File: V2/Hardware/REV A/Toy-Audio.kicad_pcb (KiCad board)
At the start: 2 copper layers, 24 x 14 mm, 24 parts, among them J1 CONN_01X02, J2 CONN_01X04, J3 CONN_01X03, J4 CONN_01X03, J5 CONN_01X04, U1 XC6206P332MR, U2 STM32F030F4P6, U3 W25Q32FVSIG, U4 TS4890

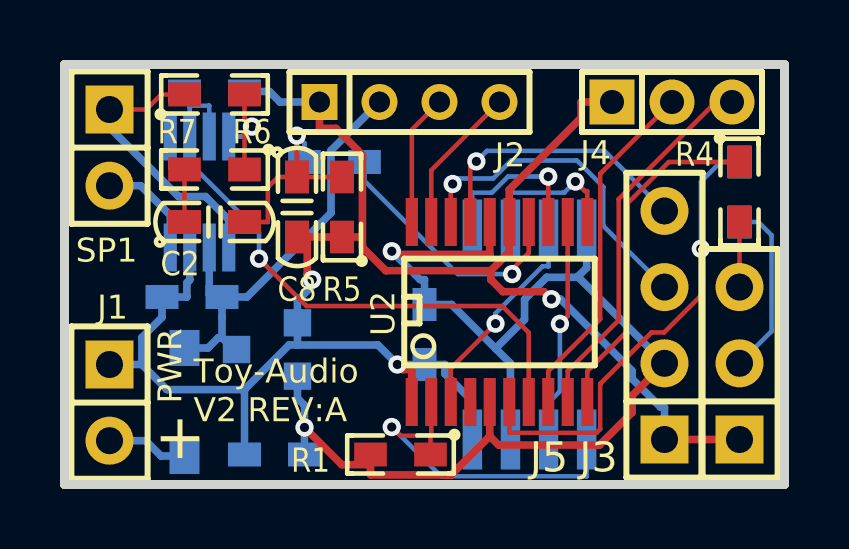
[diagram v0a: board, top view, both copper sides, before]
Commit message: Modified PCB layout, improved hand solderability.
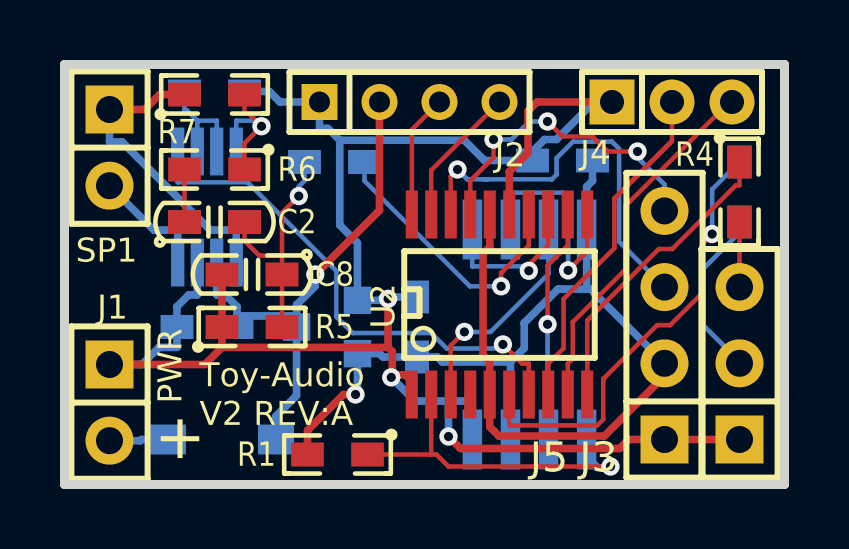
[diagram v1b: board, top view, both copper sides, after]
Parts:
- R3: value 1k8 -> 910R
- R5: value 1k8 -> D.N.P
- moved C7 7.40 mm to (112.6, 92.2), turned to 180 degrees
- moved C6 6.37 mm to (107.8, 97.8), turned to 90 degrees
- moved R5 5.00 mm to (102.2, 97.8), turned to 0 degrees
- moved C8 2.70 mm to (102.2, 96.0), turned to 180 degrees
- moved U1 2.14 mm to (104.8, 97.8)
- moved R1 2.10 mm to (105.1, 102.0)
- moved D1 1.77 mm to (101.2, 101.5), turned to 180 degrees
- moved C10 1.12 mm to (100.8, 97.8)
- moved U4 0.56 mm to (100.8, 93.8)
- moved U2 0.25 mm to (110.5, 97.0)
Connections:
- net Net-(R7-Pad1) renamed /SP+
- net Net-(SP1-Pad2) renamed /SP-
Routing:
- net GND: track 62.7 -> 66.6 mm
- net VDD: track 42.0 -> 38.6 mm, vias 2 -> 1
- net /SCK1: track 5.10 -> 7.77 mm
- net VCC: track 14.8 -> 17.3 mm, vias 0 -> 1
- net /USART1_TX: track 11.7 -> 14.2 mm
- net /SDA1: track 11.2 -> 13.3 mm
- net /SCL1: track 9.35 -> 11.1 mm, vias 1 -> 3
- net Net-(R6-Pad1): track 3.62 -> 5.00 mm
- net /LED: track 11.5 -> 10.2 mm
- net Net-(C2-Pad2): track 6.92 -> 7.89 mm
- net /SP+: track 9.48 -> 10.3 mm
- net /nMUTE: track 18.1 -> 17.3 mm
- net Net-(D1-PadA): track 2.71 -> 1.97 mm
- net Net-(C1-Pad1): track 3.25 -> 3.90 mm
- net /PWM: track 8.80 -> 9.41 mm
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
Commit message: Added Standby mode to software V1. Modified hardware to support Standby (add pull up/down resistors) todo hardware V3
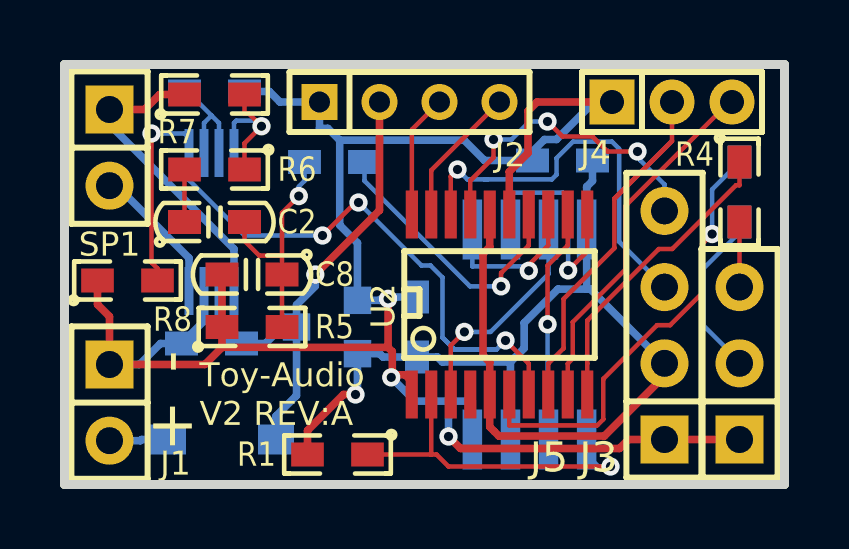
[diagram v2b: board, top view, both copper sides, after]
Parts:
- added R8: 47k, MvdL:R0603, F.Cu at (98.1, 96.2)
- U4: footprint myfootprints VDL:SSOP-8 -> MvdL:MSOP8
- moved C10 0.57 mm to (100.9, 98.3)
- moved U4 0.47 mm to (100.9, 94.2)
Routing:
- net /nMUTE: track 17.3 -> 26.9 mm, vias 1 -> 4
- net GND: track 66.6 -> 68.5 mm
- net /SP-: track 3.97 -> 4.75 mm
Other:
- board text added: "-"
- board text added: "SP1"

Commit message: Improved Wake-up pin stability WKUP1. modiefied schematic files. Software V1 is compatible with hardware V2
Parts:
- added R9: 10k, MvdL:R0603, B.Cu at (119.3, 100.8)
- R8: value 47k -> 100k
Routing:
- net GND: track 68.5 -> 71.4 mm
- net Net-(J3-Pad2): track 5.70 -> 6.83 mm
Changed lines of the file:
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@@
 (kicad_pcb (version 4) (host pcbnew 4.0.0-rc2-stable)
   (general
-    (links 59)
+    (links 61)
     (no_connects 0)
     (area 95.849999 88.849999 120.150001 103.150001)
     (thickness 1.6)
     (drawings 9)
-    (tracks 305)
+    (tracks 312)
     (zones 0)
-    (modules 25)
+    (modules 26)
     (nets 28)
   )
@@
       (effects (font (size 0.8128 0.7112) (thickness 0.1524)))
     )
-    (fp_text value 47k (at 0.0254 1.143) (layer F.Fab)
+    (fp_text value 100k (at 0.0254 1.143) (layer F.Fab)
       (effects (font (size 0.50038 0.50038) (thickness 0.10922)))
     )
@@
     )
   )
+  (module MvdL:R0603 (layer B.Cu)
+    (at 119.3 100.75 90)
+    (attr smd)
+    (fp_text reference R9 (at 3 0 360) (layer B.SilkS)
+      (effects (font (size 0.8128 0.7112) (thickness 0.1524)) (justify mirror))
+    )
+    (fp_text value 10k (at 0.0254 -1.143 90) (layer B.Fab)
+      (effects (font (size 0.50038 0.50038) (thickness 0.10922)) (justify mirror))
+    )
+    (fp_line (start -1.6002 0.635) (end -1.7272 0.635) (layer B.SilkS) (width 0.1524))
+    (fp_line (start -1.7772 0.635) (end -1.7772 -0.635) (layer B.SilkS) (width 0.1524))
+    (fp_line (start -1.7272 -0.635) (end -1.6256 -0.635) (layer B.SilkS) (width 0.1524))
+    (fp_line (start 1.6002 0.635) (end 1.7272 0.635) (layer B.SilkS) (width 0.1524))
+    (fp_line (start 1.7772 0.635) (end 1.7772 -0.635) (layer B.SilkS) (width 0.1524))
+    (fp_line (start 1.7272 -0.635) (end 1.6002 -0.635) (layer B.SilkS) (width 0.1524))
+    (fp_line (start 0.5814 0.635) (end 1.7752 0.635) (layer B.SilkS) (width 0.1524))
+    (fp_line (start 0.5814 -0.635) (end 1.7752 -0.635) (layer B.SilkS) (width 0.1524))
+    (fp_line (start -0.5564 -0.635) (end -1.7502 -0.635) (layer B.SilkS) (width 0.1524))
+    (fp_line (start -0.5814 0.635) (end -1.7752 0.635) (layer B.SilkS) (width 0.1524))
+    (fp_circle (center -1.7974 -0.658) (end -1.7974 -0.531) (layer B.SilkS) (width 0.1524))
+    (pad 1 smd rect (at -1 0 90) (size 1.0922 0.8) (layers B.Cu B.Paste B.Mask)
+      (net 1 GND) (clearance 0.1524))
+    (pad 2 smd rect (at 1 0 90) (size 1.0922 0.8) (layers B.Cu B.Paste B.Mask)
+      (net 16 "Net-(J3-Pad2)") (clearance 0.1524))
+    (model smd/chip_cms.wrl
+      (at (xyz 0 0 0))
+      (scale (xyz 0.1 0.1 0.1))
+      (rotate (xyz 0 0 0))
+    )
+  )
   (gr_text SP1 (at 98.4 94.6) (layer B.SilkS)
     (effects (font (size 0.8 0.8) (thickness 0.1524)) (justify left mirror))
@@
     (effects (font (size 1.5 1.5) (thickness 0.3)))
   )
-  (segment (start 97.1 96.2) (end 97.1 97) (width 0.254) (layer F.Cu) (net 1) (status 400000))
-  (segment (start 97.5 97.4) (end 97.5 99) (width 0.254) (layer F.Cu) (net 1) (status 800000))
+  (segment (start 118.5 101.5) (end 119.05 101.5) (width 0.254) (layer B.Cu) (net 1))
+  (segment (start 119.05 101.5) (end 119.3 101.75) (width 0.254) (layer B.Cu) (net 1))
+  (segment (start 119.3 101.75) (end 118.5 101.5) (width 0.254) (layer B.Cu) (net 1))
+  (segment (start 119.05 101.5) (end 119.3 101.75) (width 0.254) (layer B.Cu) (net 1))
+  (segment (start 119.3 101.75) (end 118.5 101.5) (width 0.254) (layer B.Cu) (net 1))
+  (segment (start 97.1 96.2) (end 97.1 97) (width 0.254) (layer F.Cu) (net 1))
+  (segment (start 97.5 97.4) (end 97.5 99) (width 0.254) (layer F.Cu) (net 1))
   (segment (start 97.1 97) (end 97.5 97.4) (width 0.254) (layer F.Cu) (net 1))
   (segment (start 99.9 98.3) (end 99.2 98.3) (width 0.254) (layer B.Cu) (net 1))
@@
   (segment (start 103.8095 93.3858) (end 103.25 93.9453) (width 0.1524) (layer F.Cu) (net 15))
   (segment (start 104 92.25) (end 104 92.8789) (width 0.1524) (layer B.Cu) (net 15))
+  (segment (start 119.3 99.75) (end 119.29 99.75) (width 0.1524) (layer B.Cu) (net 16))
+  (segment (start 119.29 99.75) (end 118.5 98.96) (width 0.1524) (layer B.Cu) (net 16))
   (segment (start 118.5 98.96) (end 118.5 98.9) (width 0.1524) (layer B.Cu) (net 16))
   (segment (start 118.5 98.9) (end 117.3 97.7) (width 0.1524) (layer B.Cu) (net 16))
@@
   (segment (start 108.875 98.368) (end 109.3294 97.9136) (width 0.1524) (layer F.Cu) (net 24))
   (segment (start 108.875 100) (end 108.875 98.368) (width 0.1524) (layer F.Cu) (net 24))
-  (segment (start 100.15 91.95) (end 100.15 91.45) (width 0.1524) (layer B.Cu) (net 25) (status C00000))
-  (segment (start 100.15 91.45) (end 100 91.3) (width 0.1524) (layer B.Cu) (net 25) (status C00000))
-  (segment (start 100 91.3) (end 98.9 91.3) (width 0.1524) (layer B.Cu) (net 25) (status 400000))
+  (segment (start 100.15 91.95) (end 100.15 91.45) (width 0.1524) (layer B.Cu) (net 25))
+  (segment (start 100.15 91.45) (end 100 91.3) (width 0.1524) (layer B.Cu) (net 25))
+  (segment (start 100 91.3) (end 98.9 91.3) (width 0.1524) (layer B.Cu) (net 25))
   (via (at 98.9 91.3) (size 0.6096) (drill 0.3048) (layers F.Cu B.Cu) (net 25))
   (segment (start 98.9 91.3) (end 98.9 94) (width 0.1524) (layer F.Cu) (net 25))
   (segment (start 98.9 94) (end 98.9 95.6) (width 0.1524) (layer F.Cu) (net 25))
-  (segment (start 98.9 95.6) (end 99.1 95.8) (width 0.1524) (layer F.Cu) (net 25) (status 800000))
-  (segment (start 99.1 95.8) (end 99.1 96.2) (width 0.1524) (layer F.Cu) (net 25) (status C00000))
+  (segment (start 98.9 95.6) (end 99.1 95.8) (width 0.1524) (layer F.Cu) (net 25))
+  (segment (start 99.1 95.8) (end 99.1 96.2) (width 0.1524) (layer F.Cu) (net 25))
   (segment (start 108.6 98.1) (end 108.6 96.1) (width 0.1524) (layer B.Cu) (net 25))
   (segment (start 110.7 98.2) (end 110.4 98.5) (width 0.1524) (layer B.Cu) (net 25))
